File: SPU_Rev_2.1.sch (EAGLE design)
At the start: 257 parts, among them Q1 12MHz

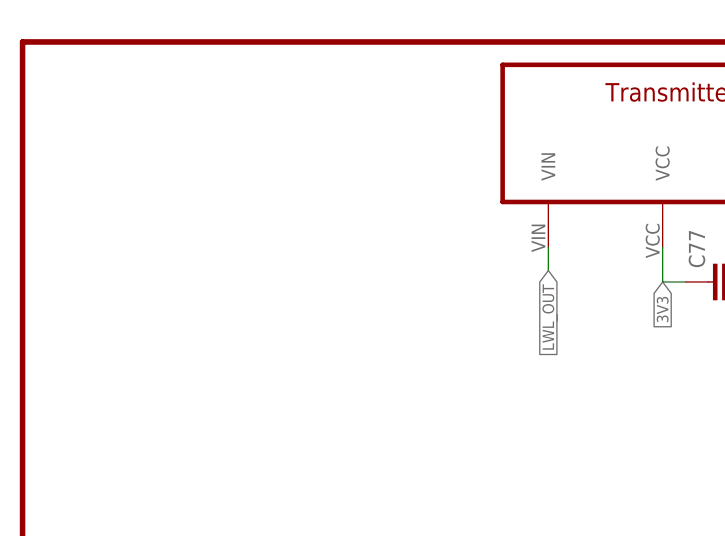
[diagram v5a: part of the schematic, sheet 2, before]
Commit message: added LWL IN
added LWL IN
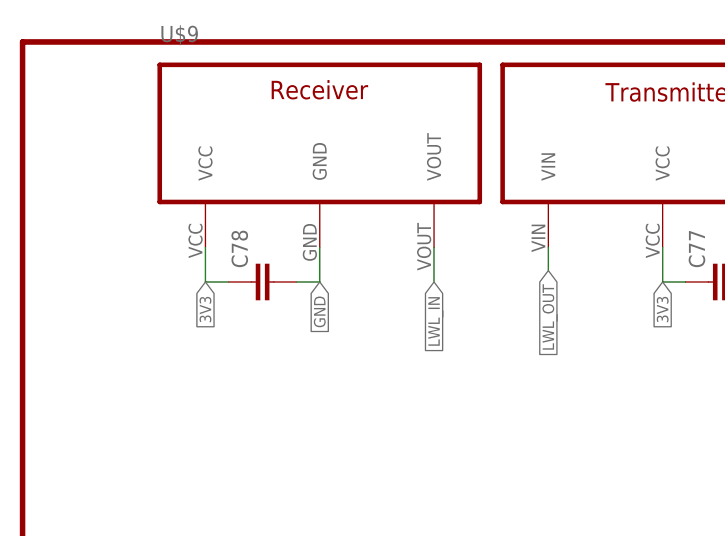
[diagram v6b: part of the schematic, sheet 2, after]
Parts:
- removed C63: 10u, rcl:CPOL-EUE/7260-38W
- added C78: (no value), rcl:C-EUC1206
- added U$9: PLR135, everlight-fiber-optics-spdif:PLR135
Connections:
- new net LWL_IN: U$9.VOUT, U_STM32F779.PI8
- net 3V3: now also C78.1, U$9.VCC
- net 5V: no longer C63.+
- net GND: now also C78.2, U$9.GND; no longer C63.-
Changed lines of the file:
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@@
 <part name="C61" library="rcl" library_urn="urn:adsk.eagle:library:334" deviceset="CPOL-EU" device="E/7260-38W" package3d_urn="urn:adsk.eagle:package:23423/1" value="10u"/>
 <part name="C62" library="rcl" library_urn="urn:adsk.eagle:library:334" deviceset="CPOL-EU" device="E/7260-38W" package3d_urn="urn:adsk.eagle:package:23423/1" value="10u"/>
-<part name="C63" library="rcl" library_urn="urn:adsk.eagle:library:334" deviceset="CPOL-EU" device="E/7260-38W" package3d_urn="urn:adsk.eagle:package:23423/1" value="10u"/>
 <part name="C64" library="rcl" library_urn="urn:adsk.eagle:library:334" deviceset="CPOL-EU" device="E/7260-38W" package3d_urn="urn:adsk.eagle:package:23423/1" value="10u"/>
 <part name="C65" library="rcl" library_urn="urn:adsk.eagle:library:334" deviceset="CPOL-EU" device="E/7260-38W" package3d_urn="urn:adsk.eagle:package:23423/1" value="10u"/>
@@
 <part name="U$8" library="everlight-fiber-optics-spdif" deviceset="PLT131" device="PLT131-T1" value="PLT131PLT131-T1"/>
 <part name="C77" library="rcl" library_urn="urn:adsk.eagle:library:334" deviceset="C-EU" device="C1206" package3d_urn="urn:adsk.eagle:package:23618/2"/>
+<part name="U$9" library="everlight-fiber-optics-spdif" deviceset="PLR135" device=""/>
+<part name="C78" library="rcl" library_urn="urn:adsk.eagle:library:334" deviceset="C-EU" device="C1206" package3d_urn="urn:adsk.eagle:package:23618/2"/>
 </parts>
 <sheets>
@@
 </segment>
 </net>
+<net name="LWL_IN" class="0">
+<segment>
+<pinref part="U_STM32F779" gate="G$1" pin="PI8"/>
+<wire x1="55.88" y1="307.34" x2="50.8" y2="307.34" width="0.1524" layer="91"/>
+<label x="50.8" y="307.34" size="1.27" layer="95" rot="R180" xref="yes"/>
+</segment>
+</net>
 </nets>
 </sheet>
@@
 <attribute name="VALUE" x="101.219" y="157.734" size="1.778" layer="96" rot="R90"/>
 </instance>
+<instance part="U$9" gate="G$1" x="53.34" y="167.64" smashed="yes">
+<attribute name="NAME" x="35.56" y="182.88" size="1.778" layer="95"/>
+</instance>
+<instance part="C78" gate="G$1" x="45.72" y="156.21" smashed="yes" rot="R90">
+<attribute name="NAME" x="45.339" y="157.734" size="1.778" layer="95" rot="R90"/>
+<attribute name="VALUE" x="50.419" y="157.734" size="1.778" layer="96" rot="R90"/>
+</instance>
 </instances>
 <busses>
@@
 <label x="104.14" y="156.21" size="1.27" layer="95" rot="R270" xref="yes"/>
 </segment>
+<segment>
+<pinref part="U$9" gate="G$1" pin="GND"/>
+<wire x1="53.34" y1="160.02" x2="53.34" y2="156.21" width="0.1524" layer="91"/>
+<pinref part="C78" gate="G$1" pin="2"/>
+<wire x1="53.34" y1="156.21" x2="50.8" y2="156.21" width="0.1524" layer="91"/>
+<label x="53.34" y="156.21" size="1.27" layer="95" rot="R270" xref="yes"/>
+</segment>
 </net>
 <net name="28V" class="0">
@@
 <label x="91.44" y="156.21" size="1.27" layer="95" rot="R270" xref="yes"/>
 </segment>
+<segment>
+<wire x1="40.64" y1="160.02" x2="40.64" y2="156.21" width="0.1524" layer="91"/>
+<wire x1="40.64" y1="156.21" x2="43.18" y2="156.21" width="0.1524" layer="91"/>
+<label x="40.64" y="156.21" size="1.27" layer="95" rot="R270" xref="yes"/>
+<pinref part="U$9" gate="G$1" pin="VCC"/>
+<pinref part="C78" gate="G$1" pin="1"/>
+</segment>
 </net>
 <net name="TDI" class="0">
@@
 </segment>
 </net>
+<net name="LWL_IN" class="0">
+<segment>
+<pinref part="U$9" gate="G$1" pin="VOUT"/>
+<wire x1="66.04" y1="156.21" x2="66.04" y2="160.02" width="0.1524" layer="91"/>
+<label x="66.04" y="156.21" size="1.27" layer="95" rot="R270" xref="yes"/>
+</segment>
+</net>
 </nets>
 </sheet>
@@
 <attribute name="VALUE" x="24.765" y="195.8086" size="1.778" layer="96"/>
 </instance>
-<instance part="C63" gate="G$1" x="101.6" y="213.36" smashed="yes">
-<attribute name="NAME" x="99.695" y="210.0834" size="1.778" layer="95" rot="R180"/>
-<attribute name="VALUE" x="99.695" y="215.6714" size="1.778" layer="96" rot="R180"/>
-</instance>
 <instance part="C64" gate="G$1" x="109.22" y="213.36" smashed="yes">
 <attribute name="NAME" x="107.315" y="210.0834" size="1.778" layer="95" rot="R180"/>
@@
 <wire x1="101.6" y1="203.2" x2="101.6" y2="205.74" width="0.1524" layer="91"/>
 <junction x="101.6" y="205.74"/>
-<pinref part="C63" gate="G$1" pin="-"/>
-<wire x1="101.6" y1="205.74" x2="101.6" y2="208.28" width="0.1524" layer="91"/>
 </segment>
 <segment>
@@
 <pinref part="C64" gate="G$1" pin="+"/>
 <wire x1="114.3" y1="215.9" x2="109.22" y2="215.9" width="0.1524" layer="91"/>
-<pinref part="C63" gate="G$1" pin="+"/>
-<wire x1="109.22" y1="215.9" x2="101.6" y2="215.9" width="0.1524" layer="91"/>
 <junction x="109.22" y="215.9"/>
-<wire x1="101.6" y1="215.9" x2="93.98" y2="215.9" width="0.1524" layer="91"/>
-<junction x="101.6" y="215.9"/>
+<wire x1="109.22" y1="215.9" x2="93.98" y2="215.9" width="0.1524" layer="91"/>
 <junction x="93.98" y="215.9"/>
 </segment>
